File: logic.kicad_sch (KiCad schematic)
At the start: 23 parts, among them J1 TC2030-IDC-NL, Q5 BSS138, U4 PIC16F15224, U8 AP63203WU

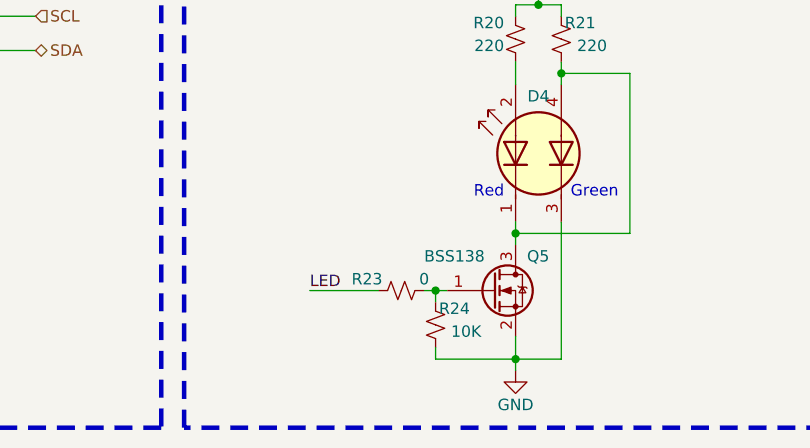
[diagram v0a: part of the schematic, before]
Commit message: Finish routing.
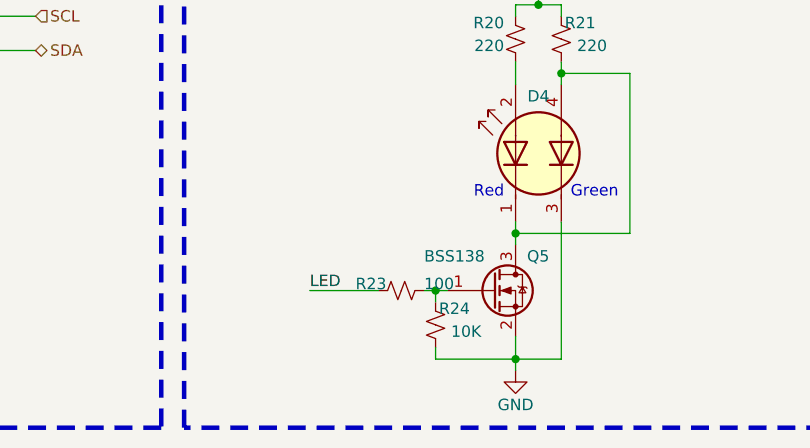
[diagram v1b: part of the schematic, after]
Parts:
- R23: value 0 -> 100; footprint Resistor_SMD:R_0603_1608Metric -> Resistor_SMD:R_0402_1005Metric; JLCPCB Footprint (none) -> 0402; MPN RMCF0603ZT0R00 -> ERJ-2RKF1000X
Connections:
- net LED: now also R23.2; no longer R23.1
- net at Q5.1 (G), R24.2: now also R23.1; no longer R23.2
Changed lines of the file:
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@@
+    )
+  )
+  (symbol (lib_id "Device:R_Small_US") (at 104.14 191.77 270) (unit 1)
+    (in_bom yes) (on_board yes) (dnp no)
+    (property "Reference" "R23" (at 99.06 191.77 90)
+      (effects (font (size 1.27 1.27)) (justify left bottom))
+    )
+    (property "Value" "100" (at 106.68 191.77 90)
+      (effects (font (size 1.27 1.27)) (justify left bottom))
+    )
+    (property "Footprint" "Resistor_SMD:R_0402_1005Metric" (at 104.14 191.77 0)
+      (effects (font (size 1.27 1.27)) hide)
+    )
+    (property "Datasheet" "~" (at 104.14 191.77 0)
+      (effects (font (size 1.27 1.27)) hide)
+    )
+    (property "MPN" "ERJ-2RKF1000X" (at 104.14 191.77 0)
+      (effects (font (size 1.27 1.27)) hide)
+    )
+    (property "Description" "" (at 104.14 191.77 0)
+      (effects (font (size 1.27 1.27)) hide)
+    )
+    (property "JLCPCB Comment" "" (at 104.14 191.77 0)
+      (effects (font (size 1.27 1.27)) hide)
+    )
+    (property "JLCPCB Footprint" "0402" (at 104.14 191.77 0)
+      (effects (font (size 1.27 1.27)) hide)
+    )
+    (pin "1")
+    (pin "2")
+    (instances
+      (project "mikona"
+        (path "/0832a6ea-8574-47f1-9003-2905bad71af2/5ee3a2c7-8940-4f63-baa3-da8fb21e9af5"
+          (reference "R23") (unit 1)
+        )
+      )
+      (project "Arm"
+        (path "/3727e59e-3d71-4d79-afcc-53b936c9d235"
+          (reference "R22") (unit 1)
+        )
+      )
     )
   )
@@
         )
       )
-    )
-  )
-  (symbol (lib_id "Device:R_Small_US") (at 104.14 191.77 90) (unit 1)
-    (in_bom yes) (on_board yes) (dnp no)
-    (property "Reference" "R23" (at 100.33 190.5 90)
-      (effects (font (size 1.27 1.27)))
-    )
-    (property "Value" "0" (at 106.68 190.5 90)
-      (effects (font (size 1.27 1.27)))
-    )
-    (property "Footprint" "Resistor_SMD:R_0603_1608Metric" (at 104.14 191.77 0)
-      (effects (font (size 1.27 1.27)) hide)
-    )
-    (property "Datasheet" "~" (at 104.14 191.77 0)
-      (effects (font (size 1.27 1.27)) hide)
-    )
-    (property "MPN" "RMCF0603ZT0R00" (at 104.14 191.77 0)
-      (effects (font (size 1.27 1.27)) hide)
-    )
-    (pin "1")
-    (pin "2")
-    (instances
-      (project "mikona"
-        (path "/0832a6ea-8574-47f1-9003-2905bad71af2/5ee3a2c7-8940-4f63-baa3-da8fb21e9af5"
-          (reference "R23") (unit 1)
-        )
-      )
-      (project "main-board"
-        (path "/5ad67b7d-c56f-4b00-8953-cc84f90f9708/e46eb433-d2d9-434e-a3d3-b851718a39e1"
-          (reference "R23") (unit 1)
-        )
-        (path "/5ad67b7d-c56f-4b00-8953-cc84f90f9708/6a867d65-34d4-44e3-a5c9-7709cd333049"
-          (reference "R501") (unit 1)
-        )
-      )

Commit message: Fix issues found during testing.
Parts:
- C11: now not fitted
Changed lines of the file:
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@@
   )
   (symbol (lib_id "Device:C_Small") (at 67.31 45.72 180) (unit 1)
-    (in_bom yes) (on_board yes) (dnp no)
+    (in_bom yes) (on_board yes) (dnp yes)
     (property "Reference" "C11" (at 72.39 43.18 0)
       (effects (font (size 1.27 1.27)) (justify left bottom))

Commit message: Use parts similar to motor-driver where possible.
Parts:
- C14, C22: MPN GMC04X7R104K50NT -> GRM155R71H104KE14J
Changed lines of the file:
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@@
       (effects (font (size 1.27 1.27)) hide)
     )
-    (property "MPN" "GMC04X7R104K50NT" (at 26.67 54.61 0)
+    (property "MPN" "GRM155R71H104KE14J" (at 26.67 54.61 0)
       (effects (font (size 1.27 1.27)) hide)
     )
@@
       (effects (font (size 1.27 1.27)) hide)
     )
-    (property "MPN" "GMC04X7R104K50NT" (at 77.47 99.06 0)
-      (effects (font (size 1.27 1.27)) hide)
-    )
+    (property "MPN" "GRM155R71H104KE14J" (at 77.47 99.06 0)
+      (effects (font (size 1.27 1.27)) hide)
+    )

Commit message: Add missing MPNs.
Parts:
- C11: MPN (none) -> 885012205067
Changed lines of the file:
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@@
       (effects (font (size 1.27 1.27)) hide)
     )
-    (property "MPN" "" (at 67.31 45.72 0)
+    (property "MPN" "885012205067" (at 67.31 45.72 0)
       (effects (font (size 1.27 1.27)) hide)
     )
-    (property "Description" "" (at 67.31 45.72 0)
+    (property "Description" "CAP CER 10000PF 50V X7R 0402" (at 67.31 45.72 0)
       (effects (font (size 1.27 1.27)) hide)
     )

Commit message: Change the parts that were not in stock.
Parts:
- C11, R22, R23: JLCPCB Footprint 0402 -> (none)
- C14, C22: JLCPCB Comment 100nF 50V X7R -> (none); JLCPCB Footprint 0402 -> (none)
- C24: JLCPCB Comment 10nF 35V X5R -> (none); JLCPCB Footprint 0603 -> (none)
- C26, C28: JLCPCB Comment 22uF 10V X5R -> (none); JLCPCB Footprint 0805 -> (none)
- FB2: JLCPCB Comment 30mΩ 100Ω@100MHz Ferrite Bead -> (none); JLCPCB Footprint 0603 -> (none)
- L2: JLCPCB Comment 3.9uH -> (none)
- R12: JLCPCB Comment 100KΩ 1% -> (none); JLCPCB Footprint 0402 -> (none)
- R2, R24: JLCPCB Comment 10KΩ -> (none); JLCPCB Footprint 0402 -> (none)
- R20, R21: JLCPCB Footprint 0402 -> (none); MPN ERJ-2RKF2200X -> ERJ-U02F2200X
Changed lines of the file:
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@@
-      (effects (font (size 1.27 1.27)) hide)
-    )
-    (property "JLCPCB Comment" "22uF 10V X5R " (at 95.25 100.33 0)
-      (effects (font (size 1.27 1.27)) hide)
-    )
-    (property "JLCPCB Footprint" "0805" (at 95.25 100.33 0)
       (effects (font (size 1.27 1.27)) hide)
     )
@@
     )
     (property "Description" "RES 100K OHM 1% 1/16W 0402" (at 171.45 38.1 0)
-      (effects (font (size 1.27 1.27)) hide)
-    )
-    (property "JLCPCB Comment" "100KΩ 1%" (at 171.45 38.1 0)
-      (effects (font (size 1.27 1.27)) hide)
-    )
-    (property "JLCPCB Footprint" "0402" (at 171.45 38.1 0)
       (effects (font (size 1.27 1.27)) hide)
     )
@@
     )
     (property "Description" "100nF 50V X7R 0402" (at 26.67 54.61 0)
-      (effects (font (size 1.27 1.27)) hide)
-    )
-    (property "JLCPCB Comment" "100nF 50V X7R" (at 26.67 54.61 0)
-      (effects (font (size 1.27 1.27)) hide)
-    )
-    (property "JLCPCB Footprint" "0402" (at 26.67 54.61 0)
       (effects (font (size 1.27 1.27)) hide)
     )
@@
       (effects (font (size 1.27 1.27)) hide)
     )
-    (property "JLCPCB Comment" "30mΩ 100Ω@100MHz Ferrite Bead" (at 31.75 96.52 0)
-      (effects (font (size 1.27 1.27)) hide)
-    )
-    (property "JLCPCB Footprint" "0603" (at 31.75 96.52 0)
-      (effects (font (size 1.27 1.27)) hide)
-    )
     (pin "1")
     (pin "2")
@@
       (effects (font (size 1.27 1.27)) hide)
     )
-    (property "JLCPCB Comment" "" (at 67.31 45.72 0)
-      (effects (font (size 1.27 1.27)) hide)
-    )
-    (property "JLCPCB Footprint" "0402" (at 67.31 45.72 0)
-      (effects (font (size 1.27 1.27)) hide)
-    )
     (pin "1")
     (pin "2")
@@
     )
     (property "Description" "" (at 63.5 99.06 0)
-      (effects (font (size 1.27 1.27)) hide)
-    )
-    (property "JLCPCB Comment" "" (at 63.5 99.06 0)
-      (effects (font (size 1.27 1.27)) hide)
-    )
-    (property "JLCPCB Footprint" "" (at 63.5 99.06 0)
       (effects (font (size 1.27 1.27)) hide)
     )
@@
       (effects (font (size 1.27 1.27)) hide)
     )
-    (property "JLCPCB Comment" "10nF 35V X5R " (at 36.83 100.33 0)
-      (effects (font (size 1.27 1.27)) hide)
-    )
-    (property "JLCPCB Footprint" "0603" (at 36.83 100.33 0)
-      (effects (font (size 1.27 1.27)) hide)
-    )
     (pin "1")
     (pin "2")
@@
       (effects (font (size 1.27 1.27)) hide)
     )
-    (property "JLCPCB Comment" "22uF 10V X5R " (at 106.68 100.33 0)
-      (effects (font (size 1.27 1.27)) hide)
-    )
-    (property "JLCPCB Footprint" "0805" (at 106.68 100.33 0)
-      (effects (font (size 1.27 1.27)) hide)
-    )
     (pin "1")
     (pin "2")
@@
     )
     (property "Description" "RES 100K OHM 1% 1/16W 0402" (at 171.45 40.64 0)
-      (effects (font (size 1.27 1.27)) hide)
-    )
-    (property "JLCPCB Comment" "100KΩ 1%" (at 171.45 40.64 0)
-      (effects (font (size 1.27 1.27)) hide)
-    )
-    (property "JLCPCB Footprint" "0402" (at 171.45 40.64 0)
       (effects (font (size 1.27 1.27)) hide)
     )
@@
       (effects (font (size 1.27 1.27)) hide)
     )
-    (property "JLCPCB Comment" "100KΩ 1%" (at 171.45 45.72 0)
-      (effects (font (size 1.27 1.27)) hide)
-    )
-    (property "JLCPCB Footprint" "0402" (at 171.45 45.72 0)
-      (effects (font (size 1.27 1.27)) hide)
-    )
     (pin "1")
     (pin "2")
@@
       (effects (font (size 1.27 1.27)) hide)
     )
-    (property "JLCPCB Comment" "" (at 73.66 40.64 0)
-      (effects (font (size 1.27 1.27)) hide)
-    )
-    (property "JLCPCB Footprint" "0402" (at 73.66 40.64 0)
-      (effects (font (size 1.27 1.27)) hide)
-    )
     (pin "1")
     (pin "2")
@@
       (effects (font (size 1.27 1.27)) hide)
     )
-    (property "JLCPCB Comment" "" (at 104.14 191.77 0)
-      (effects (font (size 1.27 1.27)) hide)
-    )
-    (property "JLCPCB Footprint" "0402" (at 104.14 191.77 0)
-      (effects (font (size 1.27 1.27)) hide)
-    )
     (pin "1")
     (pin "2")
@@
       (effects (font (size 1.27 1.27)) hide)
     )
-    (property "JLCPCB Comment" "3.9uH" (at 87.63 96.52 0)
-      (effects (font (size 1.27 1.27)) hide)
-    )
-    (property "JLCPCB Footprint" "" (at 87.63 96.52 0)
-      (effects (font (size 1.27 1.27)) hide)
-    )
     (pin "1")
     (pin "2")
@@
     )
     (property "Description" "RES 100K OHM 1% 1/16W 0402" (at 77.47 49.53 0)
-      (effects (font (size 1.27 1.27)) hide)
-    )
-    (property "JLCPCB Comment" "100KΩ 1%" (at 77.47 49.53 0)
-      (effects (font (size 1.27 1.27)) hide)
-    )
-    (property "JLCPCB Footprint" "0402" (at 77.47 49.53 0)
       (effects (font (size 1.27 1.27)) hide)
     )
@@
       (effects (font (size 1.27 1.27)) hide)
     )
-    (property "JLCPCB Comment" "10KΩ" (at 67.31 35.56 0)
-      (effects (font (size 1.27 1.27)) hide)
-    )
-    (property "JLCPCB Footprint" "0402" (at 67.31 35.56 0)
-      (effects (font (size 1.27 1.27)) hide)
-    )
     (pin "1")
     (pin "2")
@@
     )
     (property "Description" "TC2030-IDC-NL" (at 24.13 25.4 0)
-      (effects (font (size 1.27 1.27)) hide)
-    )
-    (property "JLCPCB Comment" "" (at 24.13 25.4 0)
-      (effects (font (size 1.27 1.27)) hide)
-    )
-    (property "JLCPCB Footprint" "" (at 24.13 25.4 0)
       (effects (font (size 1.27 1.27)) hide)
     )
@@
       (effects (font (size 1.27 1.27)) hide)
     )
-    (property "JLCPCB Comment" "10KΩ" (at 107.95 195.58 0)
-      (effects (font (size 1.27 1.27)) hide)
-    )
-    (property "JLCPCB Footprint" "0402" (at 107.95 195.58 0)
-      (effects (font (size 1.27 1.27)) hide)
-    )
     (pin "1")
     (pin "2")
@@
       (effects (font (size 1.27 1.27)) hide)
     )
-    (property "MPN" "ERJ-2RKF2200X" (at 116.84 163.83 0)
+    (property "MPN" "ERJ-U02F2200X" (at 116.84 163.83 0)
       (effects (font (size 1.27 1.27)) hide)
     )
     (property "Description" "" (at 116.84 163.83 0)
-      (effects (font (size 1.27 1.27)) hide)
-    )
-    (property "JLCPCB Comment" "" (at 116.84 163.83 0)
-      (effects (font (size 1.27 1.27)) hide)
-    )
-    (property "JLCPCB Footprint" "0402" (at 116.84 163.83 0)
       (effects (font (size 1.27 1.27)) hide)
     )
@@
       (effects (font (size 1.27 1.27)) hide)
     )
-    (property "MPN" "ERJ-2RKF2200X" (at 121.92 163.83 0)
+    (property "MPN" "ERJ-U02F2200X" (at 121.92 163.83 0)
       (effects (font (size 1.27 1.27)) hide)
     )
     (property "Description" "" (at 121.92 163.83 0)
-      (effects (font (size 1.27 1.27)) hide)
-    )
-    (property "JLCPCB Comment" "" (at 121.92 163.83 0)
-      (effects (font (size 1.27 1.27)) hide)
-    )
-    (property "JLCPCB Footprint" "0402" (at 121.92 163.83 0)
       (effects (font (size 1.27 1.27)) hide)
     )
@@
       (effects (font (size 1.27 1.27)) hide)
     )
-    (property "JLCPCB Comment" "100nF 50V X7R" (at 77.47 99.06 0)
-      (effects (font (size 1.27 1.27)) hide)
-    )
-    (property "JLCPCB Footprint" "0402" (at 77.47 99.06 0)
-      (effects (font (size 1.27 1.27)) hide)
-    )
